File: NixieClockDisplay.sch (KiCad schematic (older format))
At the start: 57 parts, among them J1 CONN_01X08, J2 CONN_01X03, J3 CONN_01X02, J4 CONN_02X04, J5 CONN_01X02, U1 TPIC6B595, U2 TPIC6B595, U3 TPIC6B595, U4 TPIC6B595, U5 TPIC6B595, U6 TPIC6B595, U7 WE-FDSM_DC/DC_5V

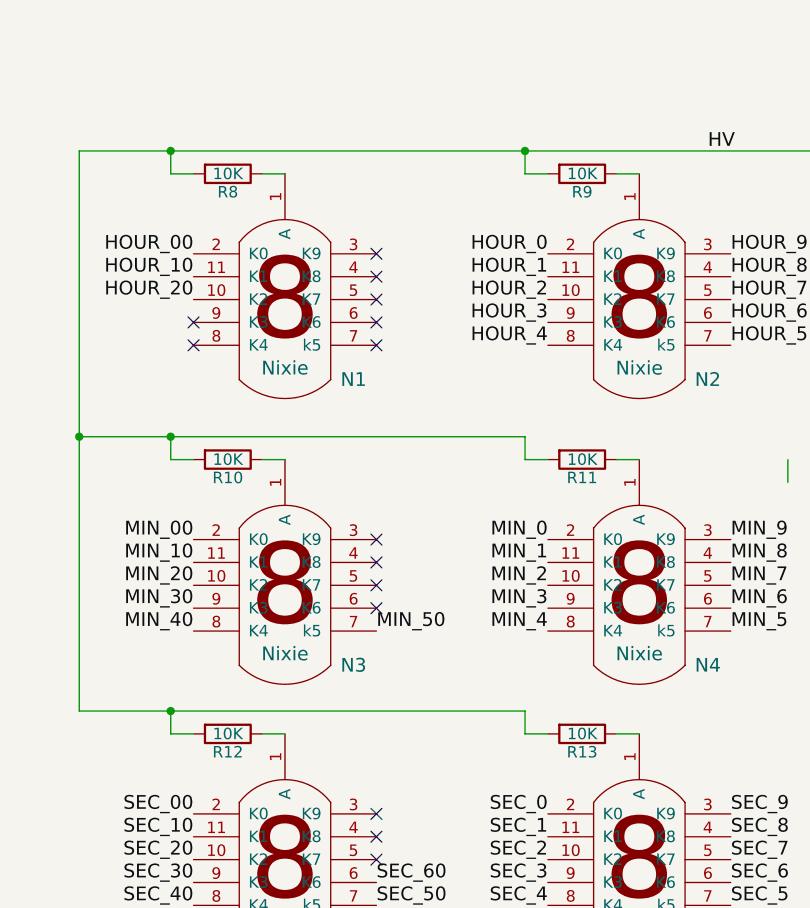
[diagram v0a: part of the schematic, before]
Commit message: Updated anode resistors; changed pin header orientation after KiCad update
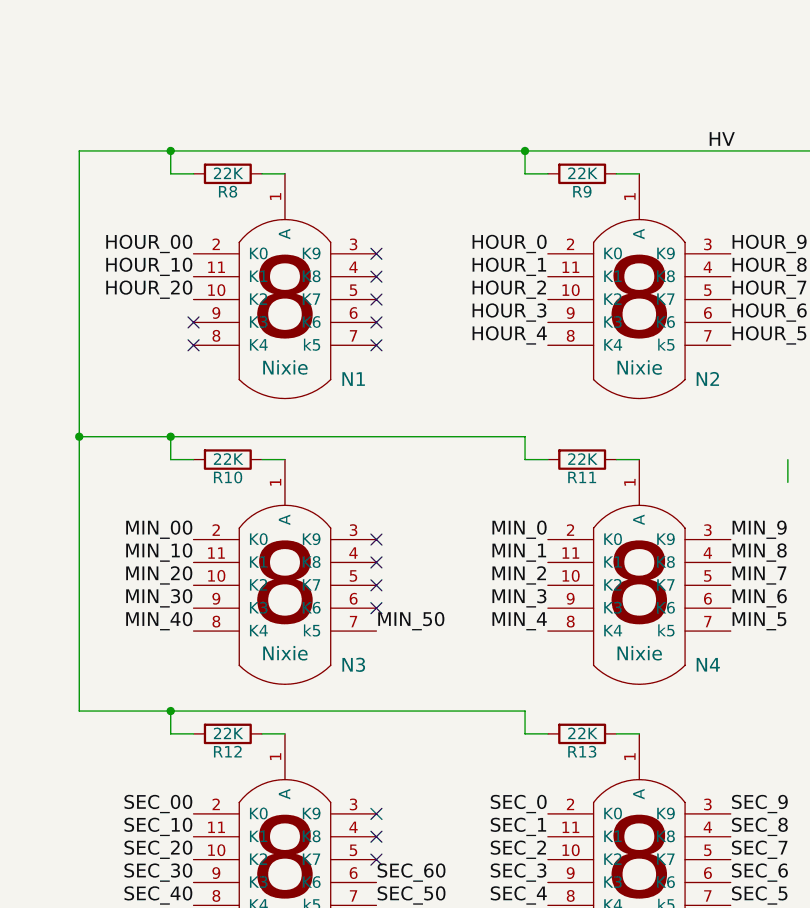
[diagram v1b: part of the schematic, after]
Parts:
- R10, R11, R12, R13, R8, R9: value 10K -> 22K
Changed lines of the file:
@@
 P 7850 800
 F 0 "R8" V 7930 800 50  0000 C CNN
-F 1 "10K" V 7850 800 50  0000 C CNN
+F 1 "22K" V 7850 800 50  0000 C CNN
 F 2 "Resistors_SMD:R_0805_HandSoldering" V 7780 800 50  0001 C CNN
 F 3 "" H 7850 800 50  0001 C CNN
@@
 P 9400 800
 F 0 "R9" V 9480 800 50  0000 C CNN
-F 1 "10K" V 9400 800 50  0000 C CNN
+F 1 "22K" V 9400 800 50  0000 C CNN
 F 2 "Resistors_SMD:R_0805_HandSoldering" V 9330 800 50  0001 C CNN
 F 3 "" H 9400 800 50  0001 C CNN
@@
 P 7850 2050
 F 0 "R10" V 7930 2050 50  0000 C CNN
-F 1 "10K" V 7850 2050 50  0000 C CNN
+F 1 "22K" V 7850 2050 50  0000 C CNN
 F 2 "Resistors_SMD:R_0805_HandSoldering" V 7780 2050 50  0001 C CNN
 F 3 "" H 7850 2050 50  0001 C CNN
@@
 P 9400 2050
 F 0 "R11" V 9480 2050 50  0000 C CNN
-F 1 "10K" V 9400 2050 50  0000 C CNN
+F 1 "22K" V 9400 2050 50  0000 C CNN
 F 2 "Resistors_SMD:R_0805_HandSoldering" V 9330 2050 50  0001 C CNN
 F 3 "" H 9400 2050 50  0001 C CNN
@@
 P 7850 3250
 F 0 "R12" V 7930 3250 50  0000 C CNN
-F 1 "10K" V 7850 3250 50  0000 C CNN
+F 1 "22K" V 7850 3250 50  0000 C CNN
 F 2 "Resistors_SMD:R_0805_HandSoldering" V 7780 3250 50  0001 C CNN
 F 3 "" H 7850 3250 50  0001 C CNN
@@
 P 9400 3250
 F 0 "R13" V 9480 3250 50  0000 C CNN
-F 1 "10K" V 9400 3250 50  0000 C CNN
+F 1 "22K" V 9400 3250 50  0000 C CNN
 F 2 "Resistors_SMD:R_0805_HandSoldering" V 9330 3250 50  0001 C CNN
 F 3 "" H 9400 3250 50  0001 C CNN

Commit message: Add Adafruit Trinket and rotary encoder.
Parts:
- removed J1: CONN_01X08, Pin_Headers:Pin_Header_Straight_1x08_Pitch2.54mm, symbol CONN_01X08
- removed J4: CONN_02X04, Pin_Headers:Pin_Header_Straight_2x04_Pitch2.54mm, symbol CONN_02X04
- removed J5: CONN_01X02, Pin_Headers:Pin_Header_Straight_1x02_Pitch2.54mm, symbol CONN_01X02
- added C17, C18, C?: .01uF, symbol C
- added C19: .1uF, Capacitors_SMD:C_0805_HandSoldering, symbol C
- added J4: Conn_02x02_Odd_Even, symbol Conn_02x02_Odd_Even
- added J5: Conn_01x04, symbol Conn_01x04
- added R14, R15, R16, R17, R?: 10K, symbol R
- added R18: 10K, Resistors_SMD:R_0805_HandSoldering, symbol R
- added R19: 100, Resistors_SMD:R_0805_HandSoldering, symbol R
- added R20: 33R, symbol R
- added SW1: RotaryEncoder_Switch_RGB, symbol RotaryEncoder_Switch_RGB
- added U8: AdafruitProTrinket5V, symbol AdafruitProTrinket5V
- added U9: WS2811, symbol WS2811
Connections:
- net labels added: HOUR_30, HOUR_40
- net labels removed: HV, PIXEL_IN, RING_IN, RING_OUT
- wire segments 280 -> 385
- no-connect marks 18 -> 15
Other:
- note added: "HV+\n\n\n\nHV-"
- note removed: "HV+\n\n\nHV-"
- moved on the sheet: C1, C10, C11, C12, C13, C14, C15, C16, C2, C3, C4, C5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

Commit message: Begin layout
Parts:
- C17, C18: footprint (none) -> Capacitors_SMD:C_0805_HandSoldering
- C20: renamed from C?; footprint (none) -> Capacitors_SMD:C_0805_HandSoldering
- J4: footprint (none) -> Pin_Headers:Pin_Header_Straight_2x02_Pitch2.54mm
- J5: footprint (none) -> Pin_Headers:Pin_Header_Straight_1x04_Pitch2.54mm
- R14, R15, R16, R17, R20: footprint (none) -> Resistors_SMD:R_0805_HandSoldering
- R21: renamed from R?; footprint (none) -> Resistors_SMD:R_0805_HandSoldering
- SW1: footprint (none) -> NixieClockDisplay:EC12PLRGB_Rotary_Encoder
- U8: footprint (none) -> NixieClockDisplay:Adafruit_Trinket_Pro
- U9: footprint (none) -> NixieClockDisplay:SOP-8
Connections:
- net labels added: /TIME_EN, TIME_IN
- wire segments 385 -> 310
- no-connect marks 15 -> 29
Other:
- moved on the sheet: C17, C20, R16, R18, R21

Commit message: Add datasheets; redraw schematic with HV5522.
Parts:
- removed C1, C2, C3, C4, C5, C6: .1uF, Capacitors_SMD:C_0805_HandSoldering, symbol C
- removed R1, R2, R3, R4, R5, R6: 10K, Resistors_SMD:R_0805_HandSoldering, symbol R
- removed SW1: RotaryEncoder_Switch_RGB, NixieClockDisplay:EC12PLRGB_Rotary_Encoder, symbol RotaryEncoder_Switch_RGB
- removed U1, U2, U3, U4, U5, U6: TPIC6B595, Housings_SOIC:SOIC-20W_7.5x12.8mm_Pitch1.27mm, symbol TPIC6B595
- removed U9: WS2811, NixieClockDisplay:SOP-8, symbol WS2811
- added J?: Conn_01x03, symbol Conn_01x03
- added J?: TEST_1P, symbol TEST_1P
- added SW?: RotaryEncoder_Switch_RGB, symbol RotaryEncoder_Switch_RGB
- added U? (x2): HV5522, symbol HV5522
- added U?: CD4504B, symbol CD4504B
- added U?: WS2811, symbol WS2811
- R16, R17, R21: value 10K -> 22K
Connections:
- net labels added: /NIXIE_BL, /NIXIE_LE, 60HZ_OUT, HOUR_50, HOUR_60, HOUR_70, HOUR_80, HOUR_90, MIN_60, MIN_70, MIN_80, MIN_90, NIXIE_CLK, NIXIE_DATA, PIXEL_DATA, ROT_A, ROT_B, ROT_PB, SEC_70, SEC_80, SEC_90
- net labels removed: /G, RCK, SRCK
- wire segments 310 -> 205
- no-connect marks 29 -> 19
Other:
- moved on the sheet: C10, C11, C12, C13, C14, C15, C16, C17, C18, C19, C20, C7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

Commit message: Replace HV5522 with HV5523
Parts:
- removed J?: TEST_1P, symbol TEST_1P
- removed U? (x2): HV5522, symbol HV5522
- removed U?: CD4504B, symbol CD4504B
- added U1, U2: HV5523, Housings_DFN_QFN:QFN-44-1EP_7x7mm_Pitch0.5mm, symbol HV5523
- J5: renamed from J?; value Conn_01x03 -> Conn_01x04; footprint (none) -> Pin_Headers:Pin_Header_Straight_1x04_Pitch2.54mm; symbol Conn_01x03 -> Conn_01x04
- SW1: renamed from SW?; footprint (none) -> NixieClockDisplay:EC12PLRGB_Rotary_Encoder
- U4: renamed from U?; footprint (none) -> Housings_SOIC:SOIC-8_3.9x4.9mm_Pitch1.27mm
- renumbered J5 to J1, U8 to U3, U7 to U5
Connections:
- net +5V: now also C8.2, J5.1 (Pin_1), LED6.4 (VDD), SW1.5, U1.27 (/POL), U1.30 (Vdd), U1.33 (/BL), U2.27 (/POL), U2.30 (Vdd), U2.33 (/BL)
- net /NIXIE_LE: now also U3.20 (PB0[8]), U1.31 (/LE), U2.31 (/LE)
- net 60HZ_OUT: now also J5.4 (Pin_4), U3.2 (PB2[10]/SS)
- net GND: now also J5.2 (Pin_2), LED1.2 (VSS), LED10.2 (VSS), LED2.2 (VSS), LED3.2 (VSS), LED4.2 (VSS), LED5.2 (VSS), LED6.2 (VSS), LED7.2 (VSS), LED8.2 (VSS), LED9.2 (VSS), U1.29 (Vss), U2.29 (Vss)
- net HOUR_0: now also U2.1 (HVOUT11)
- net HOUR_00: now also U2.11 (HVOUT21)
- net HOUR_1: now also U2.2 (HVOUT12)
- net HOUR_10: now also U2.12 (HVOUT22)
- net HOUR_2: now also U2.3 (HVOUT13)
- net HOUR_20: now also U2.13 (HVOUT23)
- net HOUR_3: now also U2.4 (HVOUT14)
- net HOUR_30: now also U2.14 (HVOUT24)
- net HOUR_4: now also U2.5 (HVOUT15)
- net HOUR_40: now also U2.15 (HVOUT25)
- net HOUR_5: now also U2.6 (HVOUT16)
- net HOUR_50: now also U2.16 (HVOUT26)
- net HOUR_6: now also U2.7 (HVOUT17)
- net HOUR_60: now also U2.17 (HVOUT27)
- net HOUR_7: now also U2.8 (HVOUT18)
- net HOUR_70: now also U2.18 (HVOUT28)
- net HOUR_8: now also U2.9 (HVOUT19)
- net HOUR_80: now also U2.19 (HVOUT29)
- net HOUR_9: now also U2.10 (HVOUT20)
- net HOUR_90: now also U2.20 (HVOUT30)
- net MIN_0: now also U1.11 (HVOUT21)
- net MIN_00: now also U2.35 (HVOUT1)
- net MIN_1: now also U1.12 (HVOUT22)
- net MIN_10: now also U2.36 (HVOUT2)
- net MIN_2: now also U1.13 (HVOUT23)
- net MIN_20: now also U2.37 (HVOUT3)
- net MIN_3: now also U1.14 (HVOUT24)
- net MIN_30: now also U2.38 (HVOUT4)
- net MIN_4: now also U1.15 (HVOUT25)
- net MIN_40: now also U2.39 (HVOUT5)
- net MIN_5: now also U1.16 (HVOUT26)
- net MIN_50: now also U2.40 (HVOUT6)
- net MIN_6: now also U1.17 (HVOUT27)
- net MIN_60: now also U2.41 (HVOUT7)
- net MIN_7: now also U1.18 (HVOUT28)
- net MIN_70: now also U2.42 (HVOUT8)
- net MIN_8: now also U1.19 (HVOUT29)
- net MIN_80: now also U2.43 (HVOUT9)
- net MIN_9: now also U1.20 (HVOUT30)
- net MIN_90: now also U2.44 (HVOUT10)
- net NIXIE_CLK: now also U1.28 (CLK), U2.28 (CLK)
- net NIXIE_DATA: now also U1.32 (DATA_IN)
- net PIXEL_DATA: now also U3.19 (PD6[6]); no longer U3.20 (PB0[8])
- net SEC_0: now also U1.35 (HVOUT1)
- net SEC_00: now also U1.1 (HVOUT11)
- net SEC_1: now also U1.36 (HVOUT2)
- net SEC_10: now also U1.2 (HVOUT12)
- net SEC_2: now also U1.37 (HVOUT3)
- net SEC_20: now also U1.3 (HVOUT13)
- net SEC_3: now also U1.38 (HVOUT4)
- net SEC_30: now also U1.4 (HVOUT14)
- net SEC_4: now also U1.39 (HVOUT5)
- net SEC_40: now also U1.5 (HVOUT15)
- net SEC_5: now also U1.40 (HVOUT6)
- net SEC_50: now also U1.6 (HVOUT16)
- net SEC_6: now also U1.41 (HVOUT7)
- net SEC_60: now also U1.7 (HVOUT17)
- net SEC_7: now also U1.42 (HVOUT8)
- net SEC_70: now also U1.8 (HVOUT18)
- net SEC_8: now also U1.43 (HVOUT9)
- net SEC_80: now also U1.9 (HVOUT19)
- net SEC_9: now also U1.44 (HVOUT10)
- net SEC_90: now also U1.10 (HVOUT20)
- net SHDN: now also U3.16 (PD3[3])
- net TIME_IN: now also U3.1 (PB1[9])
- new net: U1.23 (DATA_OUT), U2.32 (DATA_IN)
- no-connect marks 19 -> 20
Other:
- note added: "Pixel Ring\nConnector"
- moved on the sheet: C17, C18, R14, R15, R16, R17, R18, SW1

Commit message: Schematic complete
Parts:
- removed J4: Conn_02x02_Odd_Even, Pin_Headers:Pin_Header_Straight_2x02_Pitch2.54mm, symbol Conn_02x02_Odd_Even
- removed J5: Conn_01x04, Pin_Headers:Pin_Header_Straight_1x04_Pitch2.54mm, symbol Conn_01x04
- added C1, C2: .1uF, Capacitors_SMD:C_0805_HandSoldering, symbol C
- added J4: Conn_01x03, Pin_Headers:Pin_Header_Straight_1x03_Pitch2.54mm, symbol Conn_01x03
- added TP1: TEST_1P, Measurement_Points:Measurement_Point_Square-TH_Small, symbol TEST_1P
- added TP2, TP3, TP4, TP5, TP6: TEST_1P, Measurement_Points:Measurement_Point_Square-TH_Big, symbol TEST_1P
- C4: renamed from C20; value .01uF -> .1uF
- C5: renamed from C18; value .01uF -> .1uF
- C6: renamed from C17; value .01uF -> .1uF
- renumbered C13 to C10, C15 to C11, C8 to C12, C10 to C13, C12 to C14, C14 to C15, C19 to C3, C9 to C8, C11 to C9, J3 to J1, J1 to J3, R20 to R1, R8 to R10, R9 to R11, R10 to R12, R11 to R13, R12 to R14, R13 to R15, R19 to R2, R18 to R3, R21 to R4, R14 to R5, R17 to R6, R15 to R7, R16 to R8, R7 to R9, U3 to U1, U1 to U2, U2 to U3
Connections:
- net +12V: now also TP2.1
- net +5V: now also C1.1, C2.1, J4.1 (Pin_1), TP1.1
- net /NIXIE_LE: now also U1.1 (PB1[9]), TP6.1; no longer U1.20 (PB0[8])
- net 60HZ_OUT: now also U1.18 (PD5[5]), TP3.1; no longer U1.2 (PB2[10]/SS)
- net GND: now also C1.2, C2.2, J4.2 (Pin_2)
- net NIXIE_CLK: now also TP5.1
- net NIXIE_DATA: now also TP4.1
- net PIXEL_DATA: now also R1.1; no longer R1.2
- net TIME_IN: now also U1.20 (PB0[8]); no longer U1.1 (PB1[9])
- net +180V: now reaches J1.1 (P1), R10.2, R11.2, R12.2, R13.2, R14.2, R15.2
- net at LED10.1 (DOUT): now also J4.3 (Pin_3)
- net at U4.6 (DIN): now also R1.2
- net ROT_A renamed ROTARY_A
- net ROT_B renamed ROTARY_B
- net ROT_PB renamed ROTARY_PB
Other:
- note added: "High Voltage Power\nSupply Connectors"
- note added: "Receiver Module\nConnector"
- note removed: "HV+\n\n\n\nHV-"
- moved on the sheet: C6, J1, J2, J3, N1, N2, N3, N4, N5, N6, R1, R10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

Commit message: Add Adafruit OLED display
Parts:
- added TP5: TEST_1P, Measurement_Points:Measurement_Point_Square-TH_Big, symbol TEST_1P
- added U5: Adafruit_OLED_Breakout_128x96, symbol Adafruit_OLED_Breakout_128x96
- renumbered TP5 to TP6, TP6 to TP7, U5 to U6
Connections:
- net +5V: now also U5.10 (Vin)
- net /NIXIE_LE: now also U1.20 (PB0[8]); no longer U1.1 (PB1[9])
- net GND: now also U5.11 (GND)
- net SHDN: now also U1.17 (PD4[4]); no longer U1.16 (PD3[3])
- net TIME_IN: now also U1.16 (PD3[3]); no longer U1.20 (PB0[8])
- net OLED_DC: now reaches U1.10 (PC3/A3)
- net OLED_DC: now also U5.3 (DC)
- net OLED_RESET: now reaches U1.11 (PC4/A4/SDA)
- net OLED_RESET: now also U5.4 (RESET)
- net CARD_DET: now reaches U1.12 (PC5/A5/SCL)
- net CARD_DET: now also U5.8 (CD)
- net OLED_SS: now reaches U1.2 (PB2[10]/SS)
- net OLED_SS: now also U5.5 (OLEDCS)
- net MISO: now reaches U1.4 (PB4[12]/MISO)
- net MISO: now also TP5.1, U5.7 (MISO)
- net NIXIE_CLK renamed SCLK
- net SCLK: now also U5.2 (SCLK)
- net NIXIE_DATA renamed MOSI
- net MOSI: now also U5.1 (MOSI)
- new net SD_SS: U1.1 (PB1[9]), U5.6 (SDCS)
- no-connect marks 20 -> 15
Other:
- moved on the sheet: C3, C4, C5, C6, J1, J2, J3, R1, R2, R3, R4, R5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

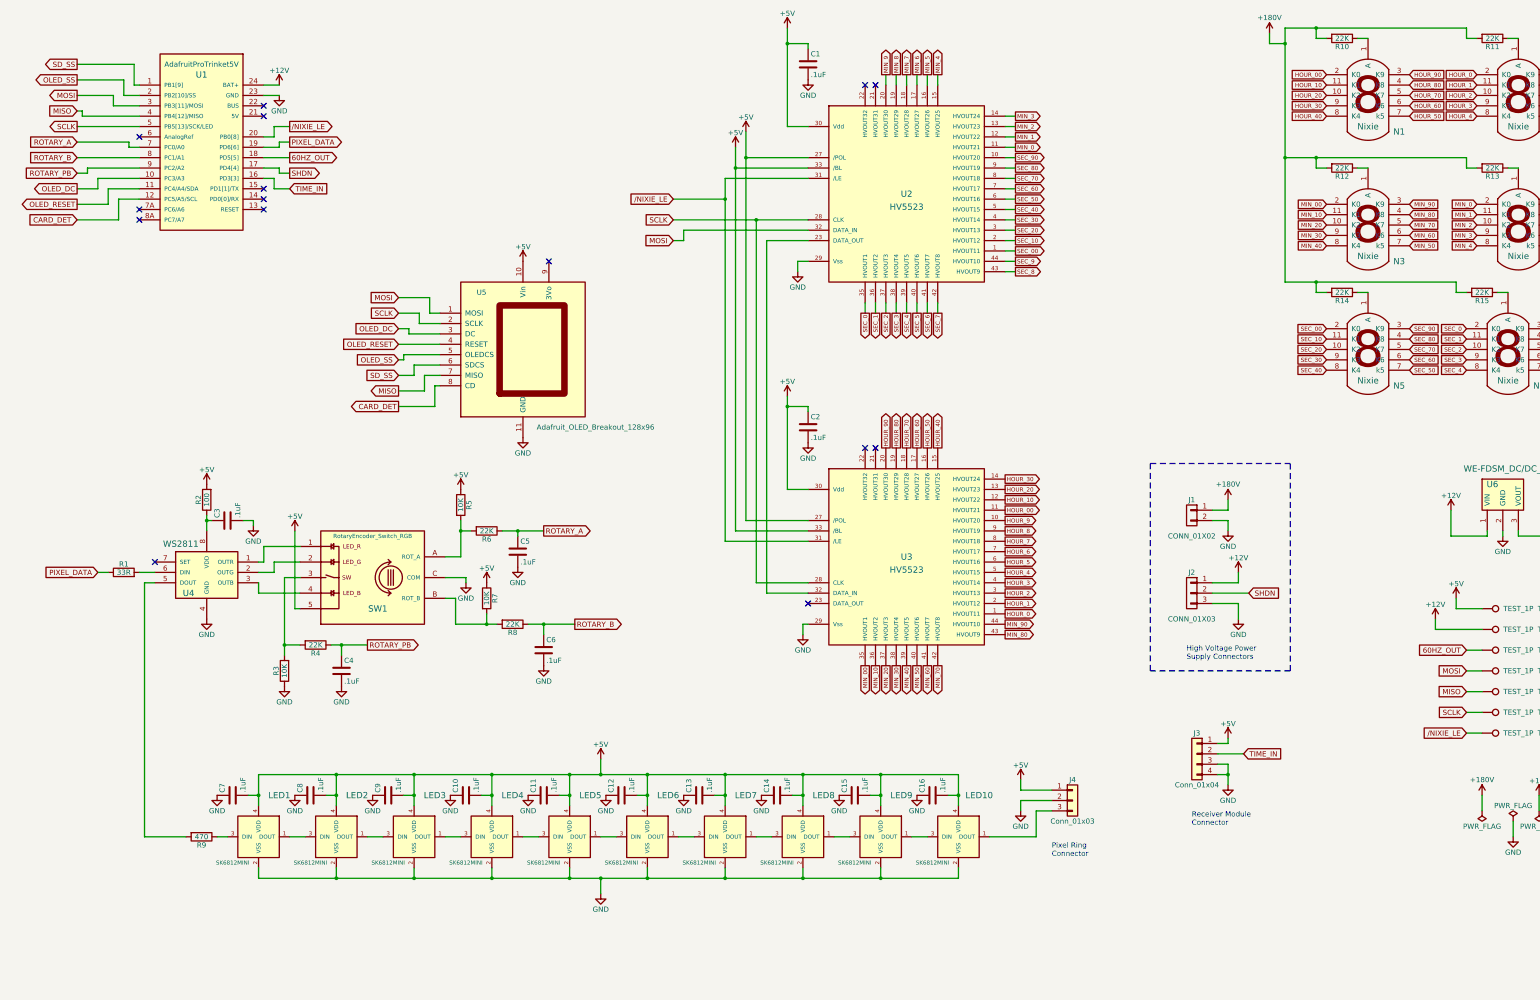
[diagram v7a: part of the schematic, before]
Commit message: Reassign PWM and TIME_IN pins
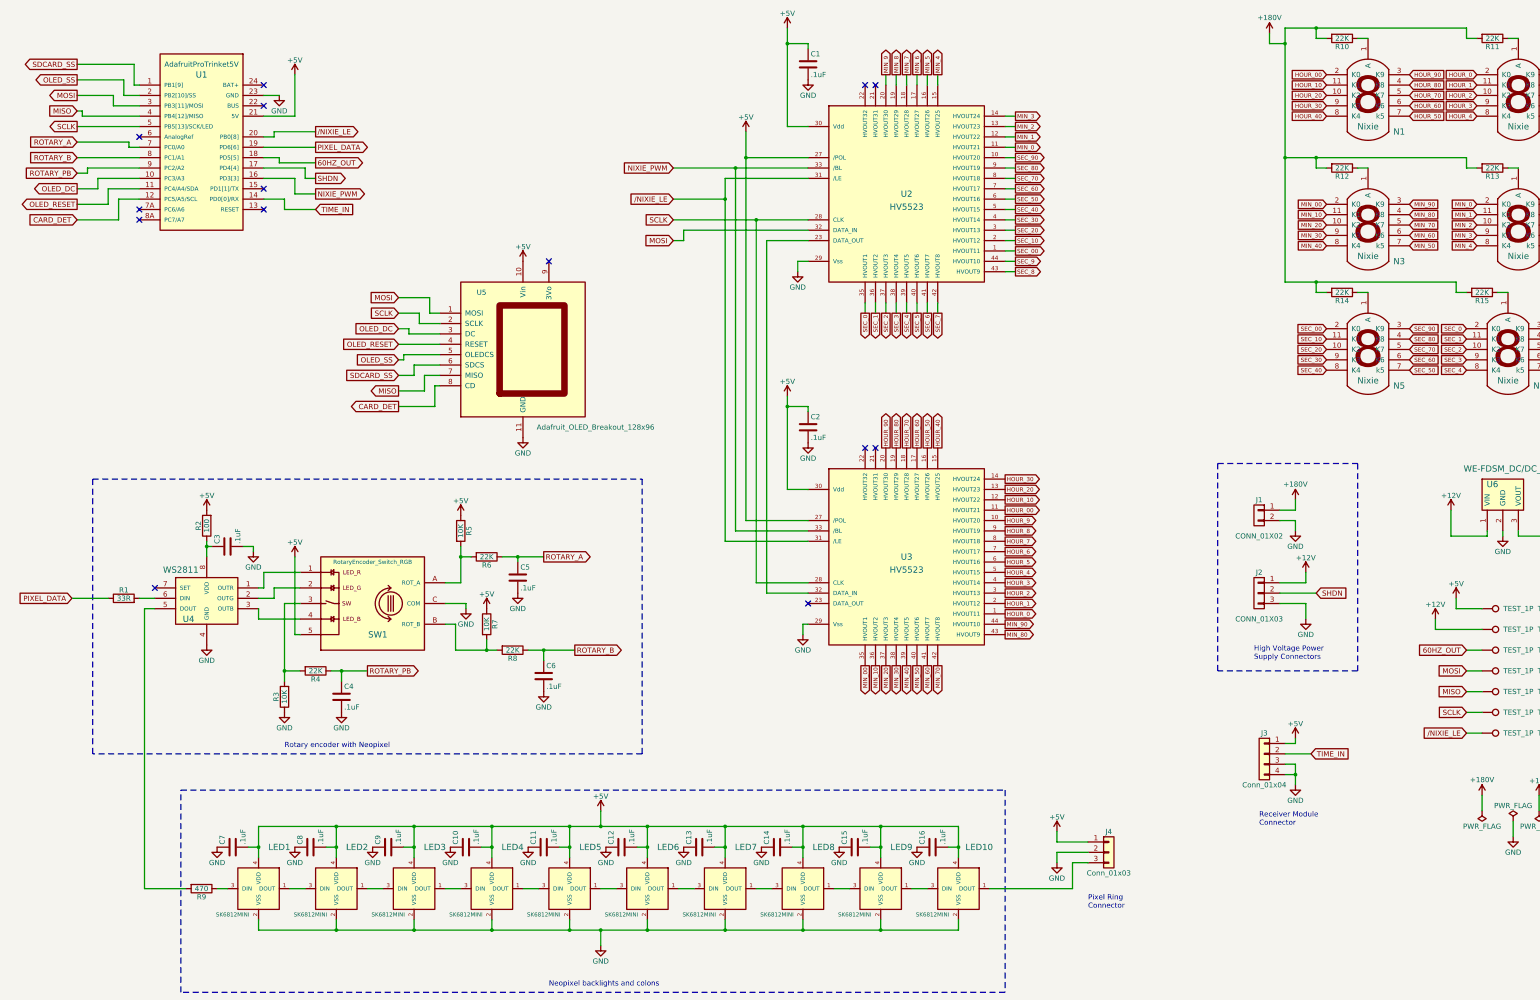
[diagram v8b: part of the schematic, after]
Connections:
- net +12V: no longer U1.24 (BAT+)
- net +5V: now also U1.21 (5V); no longer U2.33 (/BL), U3.33 (/BL)
- net TIME_IN: now also U1.14 (PD0[0]/RX); no longer U1.16 (PD3[3])
- net SD_SS renamed SDCARD_SS
- new net NIXIE_PWM: U1.16 (PD3[3]), U2.33 (/BL), U3.33 (/BL)
- no-connect marks 15 -> 14
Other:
- note added: "Neopixel backlights and colons"
- note added: "Rotary encoder with Neopixel"
- moved on the sheet: C10, C11, C12, C13, C14, C15, C16, C3, C4, C5, C6, C7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
